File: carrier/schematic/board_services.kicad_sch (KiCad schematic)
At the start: 10 parts, among them J2010 ZX-SH1.0-4PWT, U2001 24AA025E48T-I/OT, U2002 RV-3028-C7-32.768kHz-1ppm-TA-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, U2003 TPS3823-33DBVR

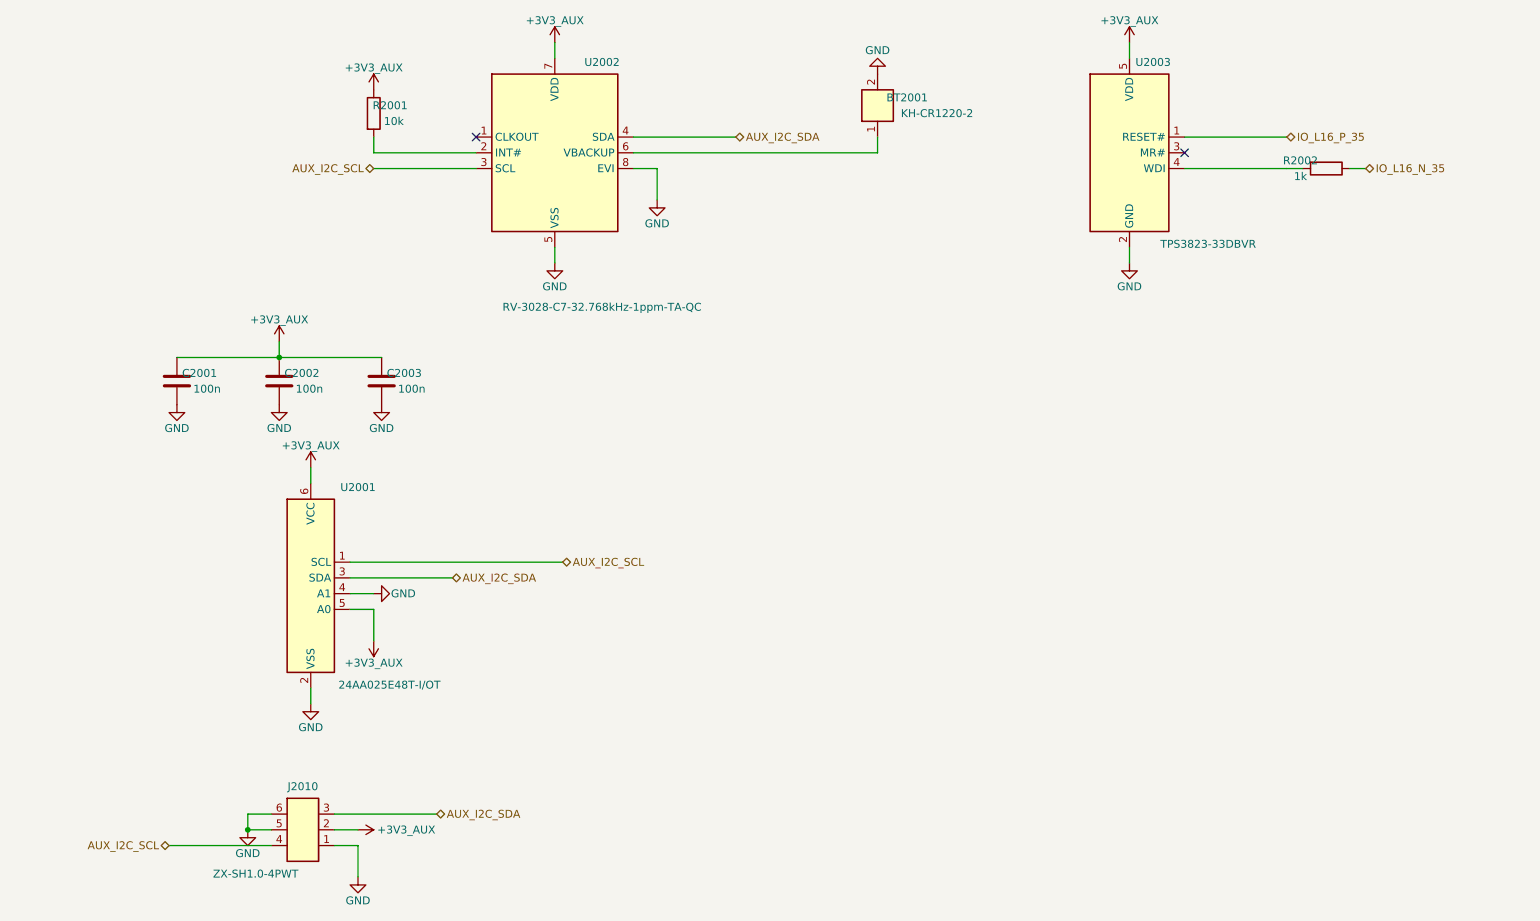
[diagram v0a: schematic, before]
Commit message: audit fixes: QWIIC ESD on its own sheet + firmware I2C-map completeness
Acting on a multi-agent adversarial re-audit of the 28-sheet board. Each
finding was independently re-verified before action — two confident "HIGH"
findings were FALSE POSITIVES whose proposed fixes would have INTRODUCED bugs,
and are documented-rejected, not applied:

  * "DSHP04 switches in parallel" — wrong. The footprint pads prove the pairing
    by physical opposition (switch n = pads n & 9-n): switch 1 = pads 1&8 is the
    only one on EN_AUX; the other even pins (2/4/6) are NC, identical to the
    proven bringup_rails SW6 idiom. The proposed "fix" (pins 1+2) wires two
    DIFFERENT switches and would leave EN_AUX permanently pulled down — the rail
    could never enable.
  * "PCA9306 EN floats when AUX is off" — wrong. A 100k to a 0 V rail pulls EN
    to 0 V (disabled), which is exactly TI's recommended "isolate when the gated
    side is unpowered" connection. No float.

REAL findings actioned:

1. QWIIC connector lacked ESD (every other external connector has it). Moved the
   QWIIC out of board_services onto its own sheet board_qwiic (the carrier's
   connectors-get-their-own-sheet idiom — rj45_connector, usb_uart_connector)
   and added a USBLC6-2SC6 low-cap ESD array at the connector (1<->6 / 3<->4
   passthrough, clamp ref +3V3_AUX). The dedicated sheet also keeps both sheets
   sparse enough for the rail-stub router. board_services drops to 9 parts.

2. schgen/firmware.py loaded only 7 sheets, so the SC-firmware contract + its
   I2C address-collision check were BLIND to the new devices. Added board_aux/
   board_services to SOURCES and three address rows: FMC-EEPROM 0x50, ID-EEPROM
   0x51 (DERIVED from the 24AA025E48 A1/A0 straps, so a mis-strap to 0x50 now
   trips the collision check against the FMC EEPROM), RTC 0x52. The firmware can
   now address the EUI-48 MAC EEPROM and the RTC. 114 -> 117 #defines.

3. board_services docstring clarified (EEPROM/RTC are on the PCA9306-i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
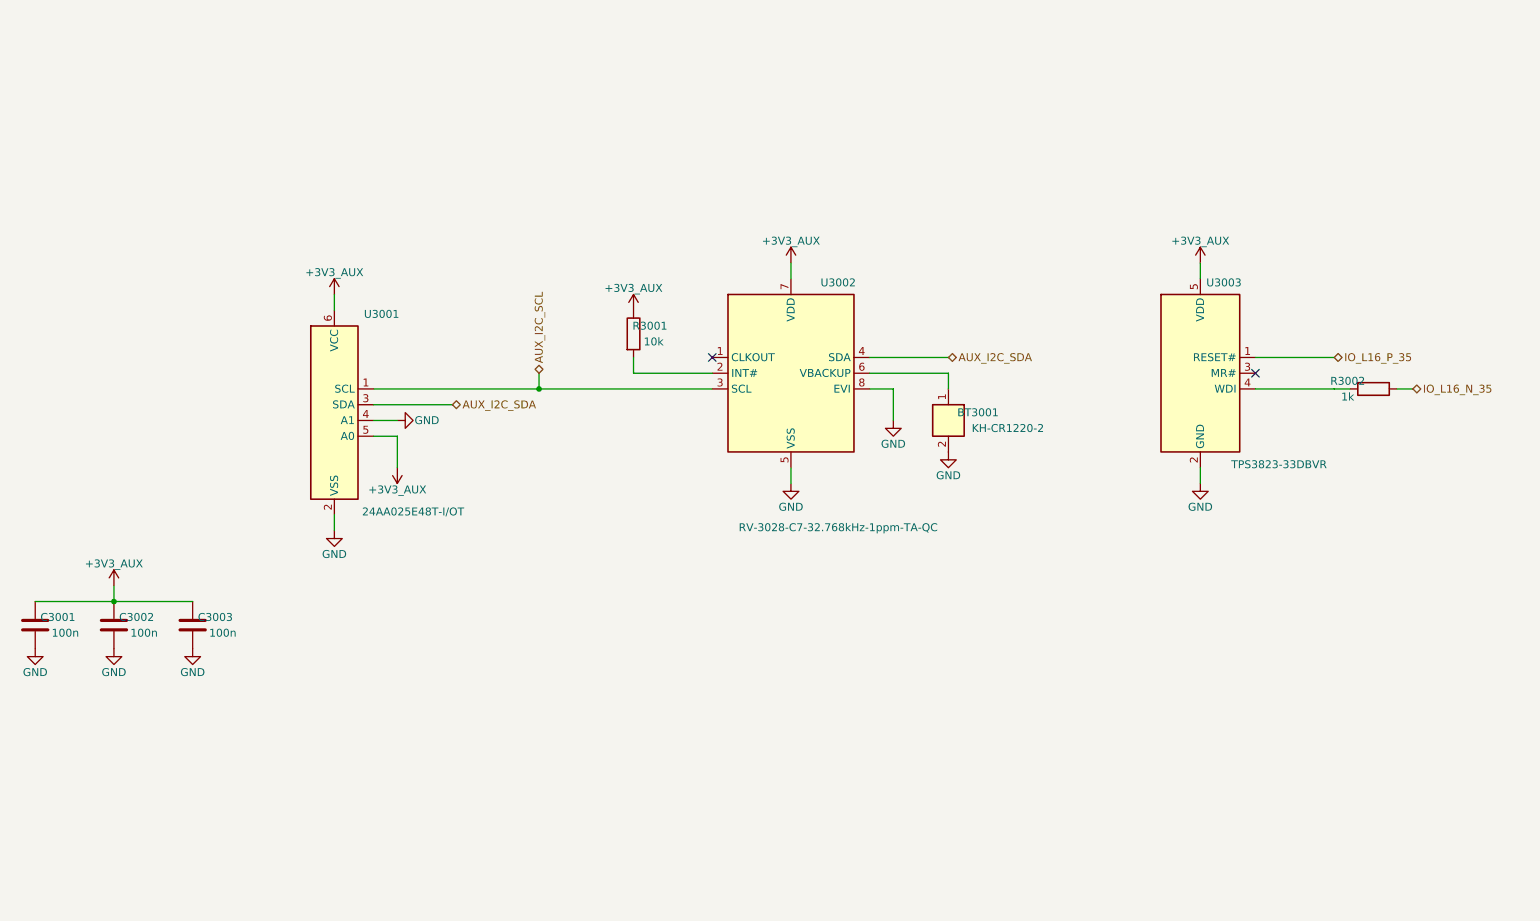
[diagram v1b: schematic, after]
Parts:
- removed J2010: ZX-SH1.0-4PWT, ZX-SH1.0-4PWT:ZX-SH1.0-4PWT, symbol ZX-SH1.0-4PWT:ZX-SH1.0-4PWT
- BT3001: renamed from U2003; value TPS3823-33DBVR -> KH-CR1220-2; footprint TPS3823-33DBVR:TPS3823-33DBVR -> KH-CR1220-2:KH-CR1220-2; symbol TPS3823-33DBVR:TPS3823-33DBVR -> KH-CR1220-2:KH-CR1220-2; LCSC C7719 -> C5365933
- C3003: renamed from U2001; value 24AA025E48T-I/OT -> 100n; footprint 24AA025E48T-I_OT:24AA025E48T-I_OT -> Capacitor_SMD:C_0603_1608Metric; symbol 24AA025E48T-I_OT:24AA025E48T-I_OT -> Device:C; LCSC C129895 -> C1591
- R3001: renamed from BT2001; value KH-CR1220-2 -> 10k; footprint KH-CR1220-2:KH-CR1220-2 -> Resistor_SMD:R_0603_1608Metric; symbol KH-CR1220-2:KH-CR1220-2 -> Device:R; LCSC C5365933 -> C25804
- R3002: renamed from C2001; value 100n -> 1k; footprint Capacitor_SMD:C_0603_1608Metric -> Resistor_SMD:R_0603_1608Metric; symbol Device:C -> Device:R; LCSC C1591 -> C21190
- U3001: renamed from U2002; value RV-3028-C7-32.768kHz-1ppm-TA-QC -> 24AA025E48T-I/OT; footprint RV-3028-C7-32.768kHz-1ppm-TA-QC:RV-3028-C7-32.768kHz-1ppm-TA-QC -> 24AA025E48T-I_OT:24AA025E48T-I_OT; symbol RV-3028-C7-32.768kHz-1ppm-TA-QC:RV-3028-C7-32.768kHz-1ppm-TA-QC -> 24AA025E48T-I_OT:24AA025E48T-I_OT; LCSC C3019759 -> C129895
- U3002: renamed from R2001; value 10k -> RV-3028-C7-32.768kHz-1ppm-TA-QC; footprint Resistor_SMD:R_0603_1608Metric -> RV-3028-C7-32.768kHz-1ppm-TA-QC:RV-3028-C7-32.768kHz-1ppm-TA-QC; symbol Device:R -> RV-3028-C7-32.768kHz-1ppm-TA-QC:RV-3028-C7-32.768kHz-1ppm-TA-QC; LCSC C25804 -> C3019759
- U3003: renamed from R2002; value 1k -> TPS3823-33DBVR; footprint Resistor_SMD:R_0603_1608Metric -> TPS3823-33DBVR:TPS3823-33DBVR; symbol Device:R -> TPS3823-33DBVR:TPS3823-33DBVR; LCSC C21190 -> C7719
- renumbered C2002 to C3001, C2003 to C3002
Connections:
- net +3V3_AUX: now also C3003.1, R3001.1, U3001.5 (A0), U3001.6 (VCC), U3002.7 (VDD), U3003.5 (VDD); no longer BT3001.5 (VDD), C3003.5 (A0), C3003.6 (VCC), R3002.1, U3001.7 (VDD), U3002.1
- net AUX_I2C_SCL: now also U3001.1 (SCL), U3002.3 (SCL); no longer C3003.1 (SCL), U3001.3 (SCL)
- net AUX_I2C_SDA: now also U3001.3 (SDA), U3002.4 (SDA); no longer C3003.3 (SDA), U3001.4 (SDA)
- net GND: now also U3001.2 (VSS), U3001.4 (A1), U3002.5 (VSS), U3002.8 (EVI), U3003.2 (GND); no longer C3003.4 (A1), R3001.2, R3002.2, U3001.5 (VSS), U3001.8 (EVI)
- net IO_L16_N_35: now also R3002.1; no longer U3003.1
- net IO_L16_P_35: now also U3003.1 (RESET#); no longer BT3001.1 (RESET#)
- net at U3002.2 (INT#): now also R3001.2; no longer U3001.2 (INT#)
- new net: R3002.2, U3003.4 (WDI)
- new net: BT3001.1, U3002.6 (VBACKUP)
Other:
- moved on the sheet: C3001, C3002

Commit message: bom: sourcing risk+cost report + C1591->C14663 (Extended->Basic 100n)
Stream F — live JLCPCB/LCSC sourcing pass over all 95 distinct BOM parts.

Report: carrier/manufacturing/SOURCING.md — per-part stock / Basic-vs-Extended
/ unit price / risk + flagged second sources, and a rollup (94 parts post-swap,
64 Extended of which 2 Preferred -> 62 feeder fees = ~$186, 15 parts <5k stock,
6 procurement-critical <300). Data from the JLCPCB parts API (live).

Applied swap (only clean Basic drop-in on the board): 100 nF 0603 decoupling
C1591 (Samsung CL10B104KB8NNNC, Extended, 2.08M) -> C14663 (YAGEO
CC0603KRX7R9BB104, Basic, 17.8M). IDENTICAL 100nF/50V/X7R/+-10%/0603, same
footprint+symbol -> netlist & render byte-identical; ratings.py already carries
C14663 with matching ratings. Merges 71 Extended + 12 existing-Basic positions
onto one 83-piece Basic line: removes one Extended feeder fee, cheaper unit,
8.5x more stock.

Everything else is REPORT-ONLY: every other Extended part is
Extended-by-necessity (no JLC-Basic equivalent — precise E96 values, specialty
ICs/connectors) or has only a footprint-mismatched / MPN-ambiguous alternate.
Also flagged (not fixed): C25750 ("40.2k" power:R1) currently resolves on LCSC
to a 120k 0402 part — a data-integrity bug; recommend C12447 after intent check.

Gates: part-rules PASS (132 checks, 0 findings); board PASS (33 sheets, golden
renders 33/33 match, DRC 0); selftest 59/59; m1_rc PASS; pytest 219 passed.
BOM regen deterministic (md5 stable).

Co-Authored-By: Claude Opus 4.8 <noreply@anthropic.com>
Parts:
- C3001, C3002, C3003: LCSC C1591 -> C14663
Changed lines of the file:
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@@
 		(property
 			"LCSC"
-			"C1591"
+			"C14663"
 			(at 30.48 120.65 0)
 			(effects
@@
 		(property
 			"LCSC"
-			"C1591"
+			"C14663"
 			(at 43.18 120.65 0)
 			(effects
@@
 		(property
 			"LCSC"
-			"C1591"
+			"C14663"
 			(at 55.88 120.65 0)
 			(effects

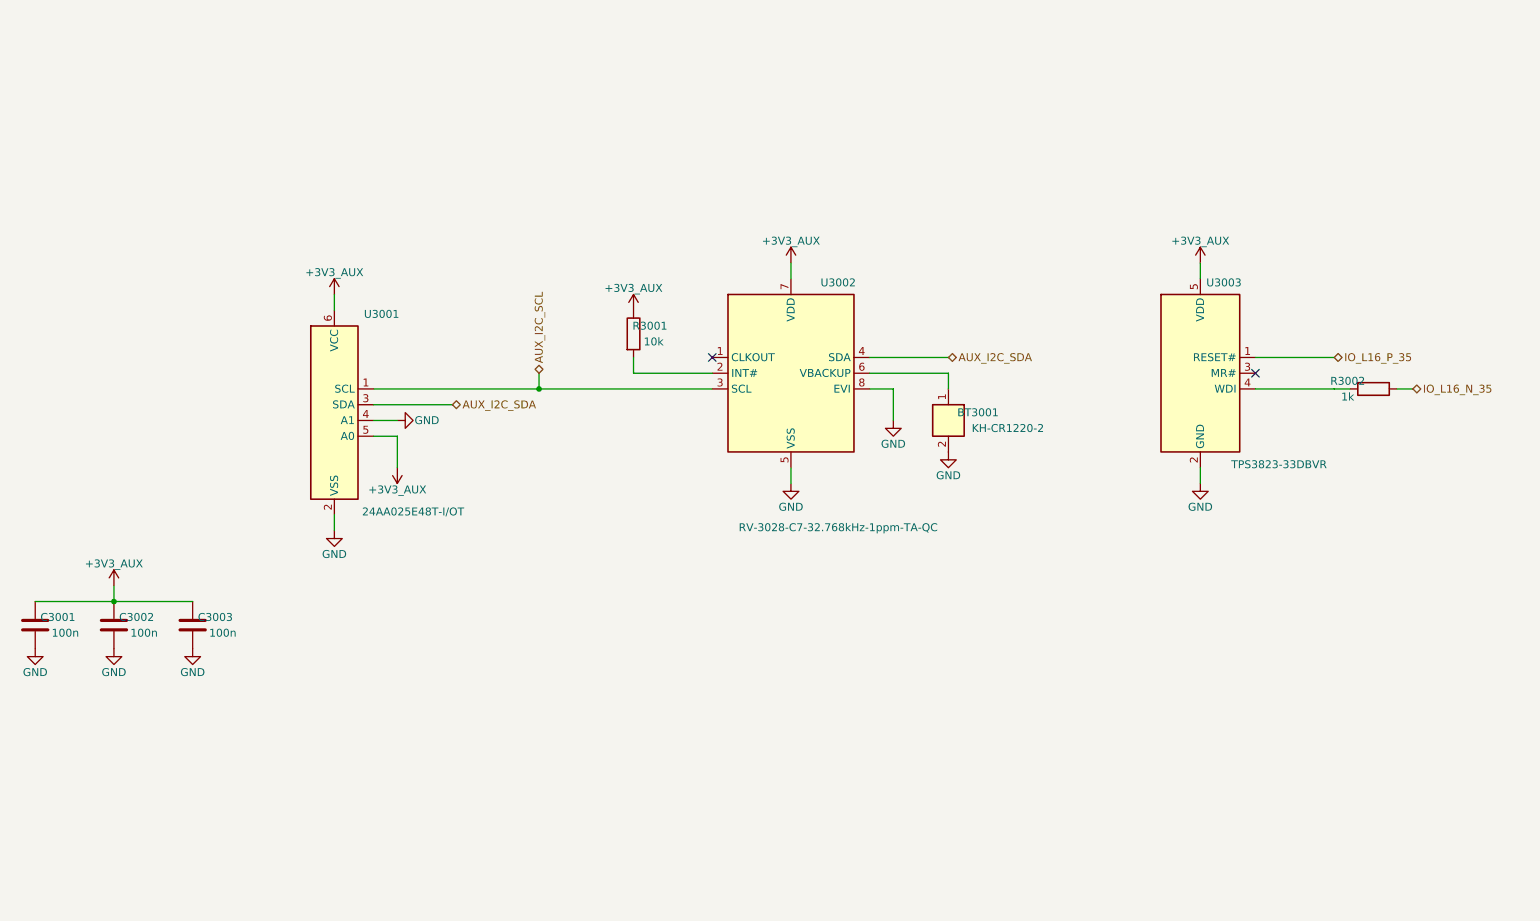
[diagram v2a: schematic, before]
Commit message: board_services: fix watchdog 3.3V->2.5V domain crossing — relocate WATCHDOG nets to a 3.3V bank (audit HIGH+MED)
The TPS3823-33 supervisor (U3, +3V3_AUX, 3.3V push-pull) drove WATCHDOG_RST_N +
WATCHDOG_KICK into Zynq bank 35 (VCCO=+2V5_VADJ): RESET# chronically forward-bit
the 2.5V input clamp diode (HIGH reliability), and the LVCMOS25 driver VOH ~2.1V
sat below the TPS3823 WDI VIH 2.31V (MED, kicks could miss).

Fix = Option A (relocate), keeping U3 on 3.3V: the TPS3823-33 MONITORS 3.3V
(VIT- 2.93V) so re-railing it to 2.5V would wedge it in reset — correctly
rejected. Moved both nets to spare bank-33 +3V3 (LVCMOS33) pins (J3.98 ball W20
RST_N, J3.96 ball W21 KICK) so they share U3's 3.3V domain: clamp gone (3.3V into
3.3V VCCO), WDI driven by LVCMOS33 VOH ~3.0V clears the 2.31V VIH.

- som_conn_gen.py: WATCHDOG_RST_N -> IO_L4_P_33, WATCHDOG_KICK -> IO_L4_N_33;
  + DO-NOT-LOAD guard comment for the on-SoM MIO VM0/VM1 straps.
- board_services.py: U3 binds the relocated nets; reset-RC waiver on the
  push-pull supervisor OUTPUT (rule not softened — LAW 4).
- XDC regenerated (LVCMOS33/bank33); manual.py + test_board_services.py updated.

Verify: LINK PASS (both nets bind board_services+som_j3); golden 33 match (only
board_services + som_j3 changed); BOARD PASS; selftest 61/61; board_services
pytest 17 passed. U3 VDD unchanged on +3V3_AUX.

Co-Authored-By: Claude Opus 4.8 <noreply@anthropic.com>
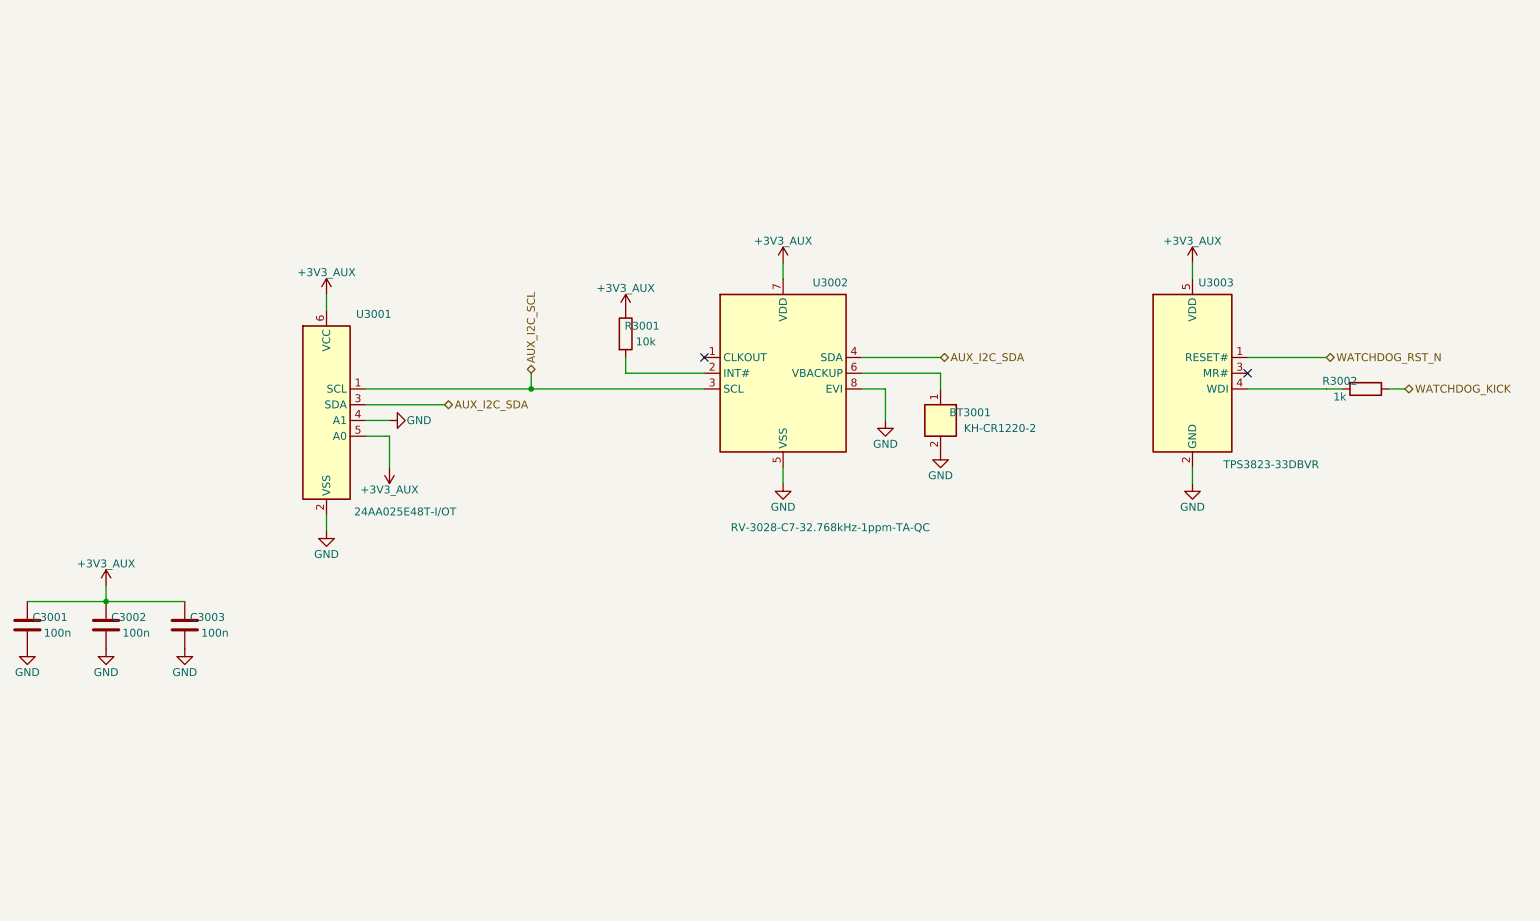
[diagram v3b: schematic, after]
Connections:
- net IO_L16_N_35 renamed WATCHDOG_KICK
- net IO_L16_P_35 renamed WATCHDOG_RST_N
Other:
- moved on the sheet: BT3001, C3001, C3002, C3003, R3001, R3002, U3001, U3002, U3003

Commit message: fix(silk): tighten 6 sheet titles overflowing the title-block cell (M6)
The audit flagged 6 sheet titles whose text overflowed the KiCad title-block
Title cell, crossing the border/zone rules (LAW 1). Root cause: the authored
Circuit titles were longer than the cell renders (the fit boundary is ~58 chars
of typical text; these were 55-73). Tightened all 6 at the source (display-only
strings, no info-loss of the essentials, cannot affect netlist/routing — board
.kicad_pcb byte-unchanged):
- board_services 73->47, pmod_expansion 65->45, mechanical 60->50,
  usb_jtag 59->38, usb_jtag_connector 58->42, power_som 55->37.
Render-confirmed: board_services + mechanical (the longest) now end well inside
the cell. The gallery description table (carrier/README.md) regenerated to match.
666 tests pass at HEAD; the 3 title-asserting tests (som_j1/j2/j3) are untouched.

Co-Authored-By: Claude Opus 4.8 <noreply@anthropic.com>
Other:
- title: Board services: ID-EEPROM(MAC) + RTC + watchdog + QWIIC on gated +3V3_AUX -> Board services: ID-EEPROM, RTC, watchdog, QWIIC
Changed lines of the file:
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@@
 	(paper "A4")
 	(title_block
-		(title "Board services: ID-EEPROM(MAC) + RTC + watchdog + QWIIC on gated +3V3_AUX")
+		(title "Board services: ID-EEPROM, RTC, watchdog, QWIIC")
 		(company "Zynq SoM Carrier")
 		(comment 1 "board_services — generated by schgen (do not hand-edit)")
